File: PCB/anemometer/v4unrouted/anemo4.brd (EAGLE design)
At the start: 100 x 80 mm, 66 parts, among them IC1 AD8223, IC2 AD8223, IC3 AD8223, IC4 AD8223, IC6 TL072D, J1 RJ12STRAIGHT-I2C, J2 RJ12STRAIGHT-I2C

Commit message: put all devices on one side on integrated bertha
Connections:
- net GND renamed AGND
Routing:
- net AGND: track 0.00 -> 27.0 mm
- added copper zone on layer 16, net N$15
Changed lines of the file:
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@@
 <wire x1="62.17" y1="70.485" x2="73.66" y2="72.26" width="0" layer="19" extent="1-1"/>
 </signal>
-<signal name="GND" class="1">
+<signal name="AGND" class="1">
 <contactref element="DIV2" pad="1"/>
 <contactref element="DIV8" pad="1"/>
@@
 <contactref element="LED0" pad="C"/>
 <contactref element="U$1" pad="5"/>
+<wire x1="31.75" y1="75.19" x2="31.75" y2="77.47" width="0.6096" layer="1"/>
+<wire x1="31.75" y1="77.47" x2="13.97" y2="77.47" width="0.6096" layer="1"/>
+<wire x1="13.97" y1="77.47" x2="13.97" y2="73.025" width="0.6096" layer="1"/>
 <wire x1="86.36" y1="66.675" x2="86.36" y2="69.215" width="0" layer="19" extent="1-1"/>
 <wire x1="78.74" y1="75.06" x2="86.36" y2="69.215" width="0" layer="19" extent="1-1"/>
@@
 <wire x1="43.18" y1="76.33" x2="46.99" y2="76.33" width="0" layer="19" extent="1-1"/>
 <wire x1="31.75" y1="75.19" x2="43.18" y2="76.33" width="0" layer="19" extent="1-1"/>
-<wire x1="24.13" y1="68.58" x2="31.75" y2="75.19" width="0" layer="19" extent="1-1"/>
-<wire x1="21.46" y1="73.66" x2="24.13" y2="68.58" width="0" layer="19" extent="16-16"/>
-<wire x1="21.46" y1="77.47" x2="21.46" y2="73.66" width="0" layer="19" extent="16-16"/>
-<wire x1="13.97" y1="73.025" x2="21.46" y2="73.66" width="0" layer="19" extent="16-16"/>
-<wire x1="13.97" y1="70.485" x2="13.97" y2="73.025" width="0" layer="19" extent="1-1"/>
+<wire x1="21.46" y1="77.47" x2="13.97" y2="77.47" width="0" layer="19" extent="1-16"/>
+<wire x1="21.46" y1="73.66" x2="21.46" y2="77.47" width="0" layer="19" extent="16-16"/>
+<wire x1="24.13" y1="68.58" x2="21.46" y2="73.66" width="0" layer="19" extent="16-16"/>
 <wire x1="30.48" y1="63.5" x2="24.13" y2="68.58" width="0" layer="19" extent="1-1"/>
 <wire x1="64.9" y1="53.34" x2="68.35" y2="64.77" width="0" layer="19" extent="1-16"/>
 <wire x1="65.405" y1="50.74" x2="64.9" y2="53.34" width="0" layer="19" extent="1-16"/>
 <wire x1="73.66" y1="50.93" x2="65.405" y2="50.74" width="0" layer="19" extent="1-1"/>
-<wire x1="86.49" y1="53.34" x2="73.66" y2="50.93" width="0" layer="19" extent="1-16"/>
-<wire x1="86.995" y1="50.74" x2="86.49" y2="53.34" width="0" layer="19" extent="1-16"/>
 <wire x1="30.48" y1="50.93" x2="30.48" y2="63.5" width="0" layer="19" extent="1-1"/>
 <wire x1="22.225" y1="50.74" x2="30.48" y2="50.93" width="0" layer="19" extent="1-1"/>
 <wire x1="21.72" y1="53.34" x2="22.225" y2="50.74" width="0" layer="19" extent="1-16"/>
+<wire x1="86.49" y1="53.34" x2="73.66" y2="50.93" width="0" layer="19" extent="1-16"/>
+<wire x1="86.995" y1="50.74" x2="86.49" y2="53.34" width="0" layer="19" extent="1-16"/>
 <wire x1="52.07" y1="50.93" x2="64.9" y2="53.34" width="0" layer="19" extent="1-16"/>
 <wire x1="43.815" y1="50.74" x2="52.07" y2="50.93" width="0" layer="19" extent="1-1"/>
@@
 <wire x1="20.45" y1="30.48" x2="22.225" y2="50.74" width="0" layer="19" extent="1-16"/>
 <wire x1="20.45" y1="16.51" x2="20.45" y2="30.48" width="0" layer="19" extent="16-16"/>
+<wire x1="13.97" y1="73.025" x2="13.97" y2="70.485" width="0.6096" layer="1"/>
 </signal>
 <signal name="IN+1">
@@
 <wire x1="71.35" y1="64.77" x2="74.8" y2="64.77" width="0" layer="19" extent="1-1"/>
 </signal>
+<signal name="N$15">
+<polygon width="0.6096" layer="16" isolate="0.3048" orphans="yes">
+<vertex x="0" y="80.01"/>
+<vertex x="99.695" y="80.01"/>
+<vertex x="99.695" y="0"/>
+<vertex x="0" y="0"/>
+</polygon>
+</signal>
 </signals>

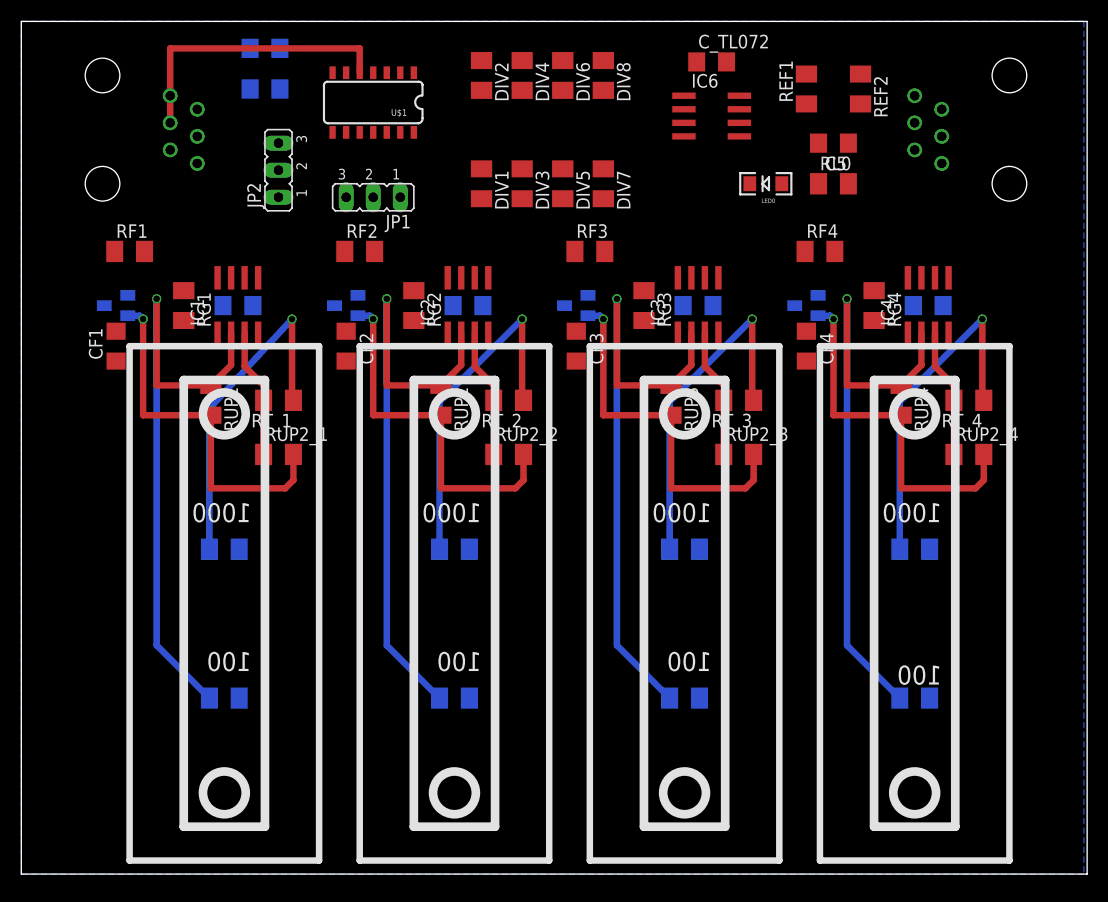
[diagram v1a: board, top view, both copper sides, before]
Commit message: routed anemometer and integrated bertha with ground planes and separate analog and digital ground. ready for fabrication
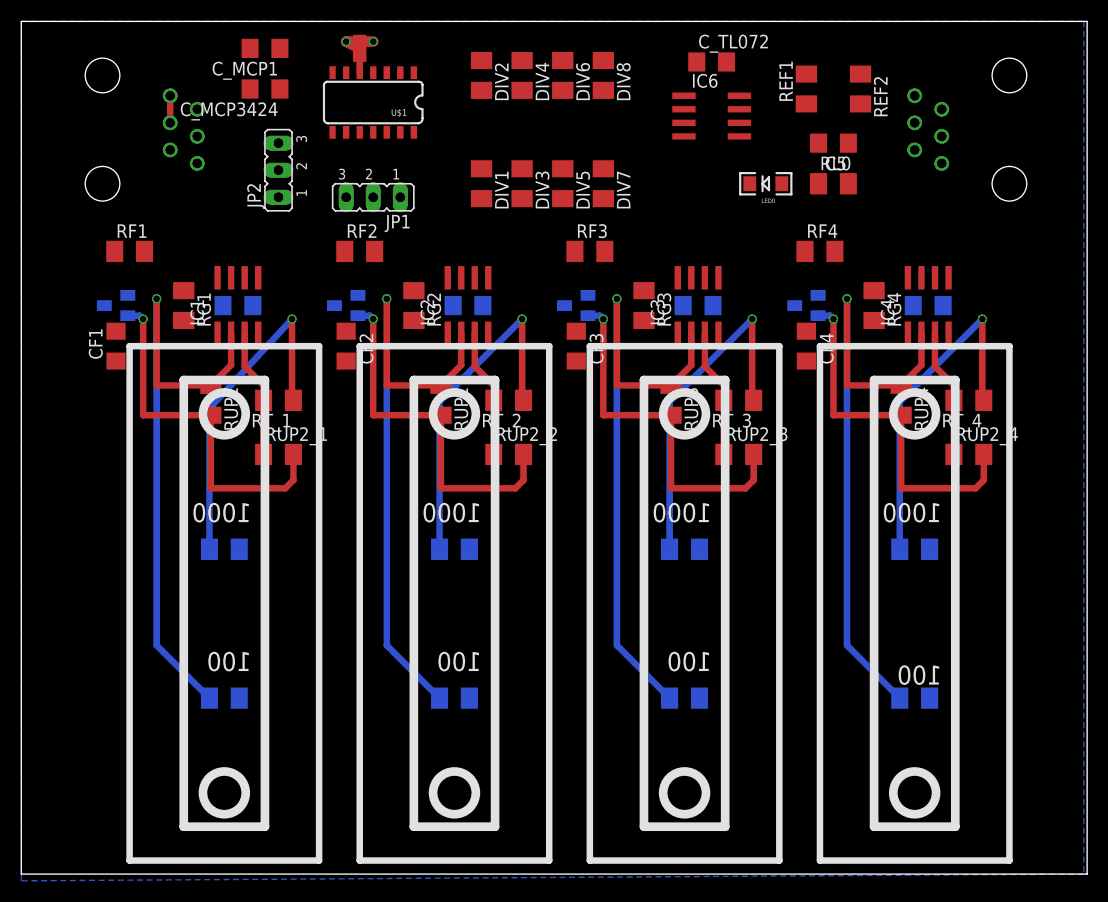
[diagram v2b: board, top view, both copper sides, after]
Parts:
- added U$2: STARGND, lpatiny:STAR
- flipped C_MCP1 to the top
- flipped C_MCP3424 to the top
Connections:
- removed net AGND: C1.2, C2.2, C3.2, C4.2, C5.2, CF1.1, CF2.1, CF3.1, CF4.1, C_MCP1.1, C_MCP3424.1, C_TL072.1, DIV2.1, DIV4.1, DIV6.1, DIV8.1, IC1.4, IC2.4, IC3.4, IC4.4, IC6.4, J1.GND1, J1.GND2, J2.GND1, J2.GND2, JP1.3, JP2.3, LED0.C, PT100_1.1, PT100_2.1, PT100_3.1, PT100_4.1, PT1K_1.1, PT1K_2.1, PT1K_3.1, PT1K_4.1, REF2.1, U$1.5
- new net DGND: U$1.5, U$2.DGND
- new net GND: C1.2, C2.2, C3.2, C4.2, C5.2, CF1.1, CF2.1, CF3.1, CF4.1, C_MCP1.1, C_MCP3424.1, C_TL072.1, DIV2.1, DIV4.1, DIV6.1, DIV8.1, IC1.4, IC2.4, IC3.4, IC4.4, IC6.4, J1.GND1, J1.GND2, J2.GND1, J2.GND2, JP1.3, JP2.3, LED0.C, PT100_1.1, PT100_2.1, PT100_3.1, PT100_4.1, PT1K_1.1, PT1K_2.1, PT1K_3.1, PT1K_4.1, REF2.1, U$2.AGND, U$2.GND
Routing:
- net AGND: track 27.0 -> 0.00 mm
- net GND: track 0.00 -> 7.13 mm, vias 0 -> 2
- net DGND: track 0.00 -> 2.92 mm
- added copper zone on layer 16, net GND
- removed copper zone on layer 16, net N$15

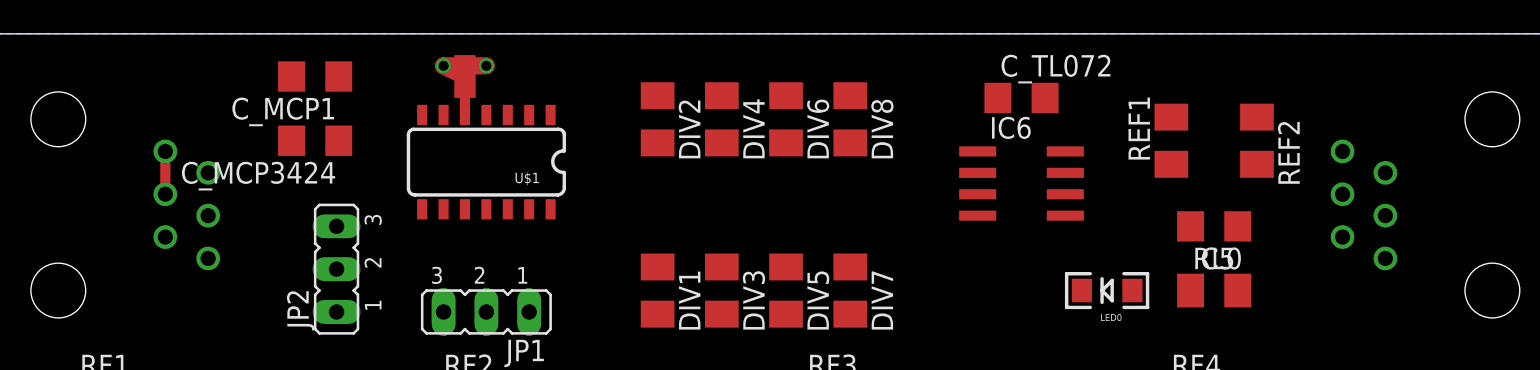
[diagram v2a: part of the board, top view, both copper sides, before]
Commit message: integratedBertha v1.1: adjusted labels to good position. Anemometer: added ferrite bead for vcc decoupling and ground line.
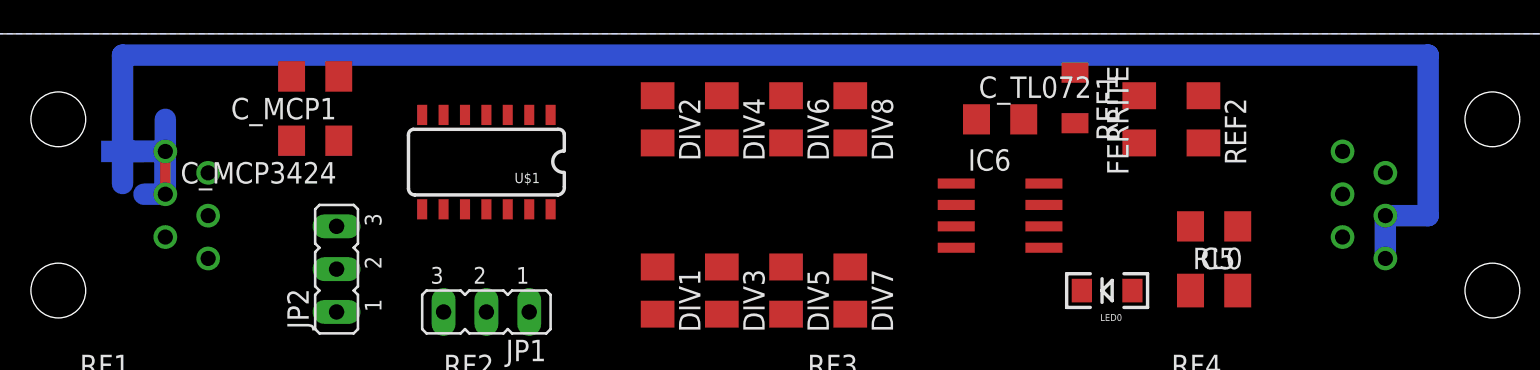
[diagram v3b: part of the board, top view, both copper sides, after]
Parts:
- added FERRITE: 80Ohm, rcl:L3216C
- moved U$2 20.1 mm to (11.4, 73.7), flipped to the bottom, turned to 270 degrees
- moved REF2 3.42 mm to (75.6, 74.9)
- moved REF1 2.29 mm to (71.8, 74.9)
- moved IC6 2.29 mm to (63.5, 69.2)
- moved C_TL072 1.80 mm to (63.5, 74.9)
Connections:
- removed net DGND: U$1.5, U$2.DGND
- new net +12V: FERRITE.1, J1.+12V, J2.+12V
- new net MIXEDGND: J1.GND1, J1.GND2, J2.GND1, J2.GND2, U$2.GND
- net GND: now also U$1.5; no longer J1.GND1, J1.GND2, J2.GND1, J2.GND2, U$2.GND
- net VCC: now also FERRITE.2; no longer J1.+12V, J2.+12V
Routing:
- net MIXEDGND: track 0.00 -> 105.4 mm
- net GND: track 7.13 -> 10.2 mm, vias 2 -> 0
- net DGND: track 2.92 -> 0.00 mm

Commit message: changed some labels, corrected C16 value in bertha. created BOM
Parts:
- PT100_1, PT100_2, PT100_3, PT100_4: value 90.9 -> PT100
- PT1K_1, PT1K_2, PT1K_3, PT1K_4: value 90.9 -> PT1000
- RG1, RG2, RG3, RG4: value 91 -> 91 0.1%
- RT_1, RT_2, RT_3, RT_4: value 90.9 -> 91 0.1%
- RUP1, RUP2, RUP3, RUP4: value 10 -> 10 0.1%
- RUP2_1, RUP2_2, RUP2_3, RUP2_4: value 100 -> 100 0.1%
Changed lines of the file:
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@@
 </autorouter>
 <elements>
-<element name="RG1" library="resistor" package="M1206" value="91" x="15.24" y="53.34" rot="R270"/>
-<element name="RUP1" library="resistor" package="M1206" value="10" x="17.78" y="44.45" rot="R270"/>
-<element name="RG2" library="resistor" package="M1206" value="91" x="36.83" y="53.34" rot="R270"/>
-<element name="RG3" library="resistor" package="M1206" value="91" x="58.42" y="53.34" rot="R270"/>
-<element name="RG4" library="resistor" package="M1206" value="91" x="80.01" y="53.34" rot="R270"/>
-<element name="RUP2" library="resistor" package="M1206" value="10" x="39.37" y="44.45" rot="R270"/>
-<element name="RUP3" library="resistor" package="M1206" value="10" x="60.96" y="44.45" rot="R270"/>
-<element name="RUP4" library="resistor" package="M1206" value="10" x="82.55" y="44.45" rot="R270"/>
-<element name="RUP2_1" library="resistor" package="M1206" value="100" x="24.13" y="39.37"/>
-<element name="RUP2_2" library="resistor" package="M1206" value="100" x="45.72" y="39.37"/>
-<element name="RUP2_3" library="resistor" package="M1206" value="100" x="67.31" y="39.37"/>
-<element name="RUP2_4" library="resistor" package="M1206" value="100" x="88.9" y="39.37"/>
+<element name="RG1" library="resistor" package="M1206" value="91 0.1%" x="15.24" y="53.34" rot="R270"/>
+<element name="RUP1" library="resistor" package="M1206" value="10 0.1%" x="17.78" y="44.45" rot="R270"/>
+<element name="RG2" library="resistor" package="M1206" value="91 0.1%" x="36.83" y="53.34" rot="R270"/>
+<element name="RG3" library="resistor" package="M1206" value="91 0.1%" x="58.42" y="53.34" rot="R270"/>
+<element name="RG4" library="resistor" package="M1206" value="91 0.1%" x="80.01" y="53.34" rot="R270"/>
+<element name="RUP2" library="resistor" package="M1206" value="10 0.1%" x="39.37" y="44.45" rot="R270"/>
+<element name="RUP3" library="resistor" package="M1206" value="10 0.1%" x="60.96" y="44.45" rot="R270"/>
+<element name="RUP4" library="resistor" package="M1206" value="10 0.1%" x="82.55" y="44.45" rot="R270"/>
+<element name="RUP2_1" library="resistor" package="M1206" value="100 0.1%" x="24.13" y="39.37"/>
+<element name="RUP2_2" library="resistor" package="M1206" value="100 0.1%" x="45.72" y="39.37"/>
+<element name="RUP2_3" library="resistor" package="M1206" value="100 0.1%" x="67.31" y="39.37"/>
+<element name="RUP2_4" library="resistor" package="M1206" value="100 0.1%" x="88.9" y="39.37"/>
 <element name="REF1" library="resistor" package="M1206" value="200k" x="71.755" y="74.93" rot="R90"/>
 <element name="REF2" library="resistor" package="M1206" value="100k" x="75.565" y="74.93" rot="R270"/>
-<element name="RT_1" library="resistor" package="M1206" value="90.9" x="24.13" y="44.45" rot="R180"/>
-<element name="RT_2" library="resistor" package="M1206" value="90.9" x="45.72" y="44.45" rot="R180"/>
-<element name="RT_3" library="resistor" package="M1206" value="90.9" x="67.31" y="44.45" rot="R180"/>
-<element name="RT_4" library="resistor" package="M1206" value="90.9" x="88.9" y="44.45" rot="R180"/>
+<element name="RT_1" library="resistor" package="M1206" value="91 0.1%" x="24.13" y="44.45" rot="R180"/>
+<element name="RT_2" library="resistor" package="M1206" value="91 0.1%" x="45.72" y="44.45" rot="R180"/>
+<element name="RT_3" library="resistor" package="M1206" value="91 0.1%" x="67.31" y="44.45" rot="R180"/>
+<element name="RT_4" library="resistor" package="M1206" value="91 0.1%" x="88.9" y="44.45" rot="R180"/>
 <element name="RF1" library="resistor" package="M1206" value="100" x="10.16" y="58.42"/>
 <element name="RF2" library="resistor" package="M1206" value="100" x="31.75" y="58.42"/>
@@
 <element name="C_MCP1" library="rcl" package="C1206" value="10µ" x="22.86" y="77.47" rot="R180"/>
 <element name="U$1" library="mcp3424" package="14LDSOIC" value="MCP3424(SO14)" x="33.02" y="72.39" rot="R270"/>
-<element name="PT1K_1" library="resistor" package="M1206" value="90.9" x="19.05" y="30.48" rot="MR0"/>
-<element name="PT100_1" library="resistor" package="M1206" value="90.9" x="19.05" y="16.51" rot="MR0"/>
-<element name="PT100_2" library="resistor" package="M1206" value="90.9" x="40.64" y="16.51" rot="MR0"/>
-<element name="PT100_3" library="resistor" package="M1206" value="90.9" x="62.23" y="16.51" rot="MR0"/>
-<element name="PT100_4" library="resistor" package="M1206" value="90.9" x="83.82" y="16.51" rot="MR0"/>
-<element name="PT1K_2" library="resistor" package="M1206" value="90.9" x="40.64" y="30.48" rot="MR0"/>
-<element name="PT1K_3" library="resistor" package="M1206" value="90.9" x="62.23" y="30.48" rot="MR0"/>
-<element name="PT1K_4" library="resistor" package="M1206" value="90.9" x="83.82" y="30.48" rot="MR0"/>
+<element name="PT1K_1" library="resistor" package="M1206" value="PT1000" x="19.05" y="30.48" rot="MR0"/>
+<element name="PT100_1" library="resistor" package="M1206" value="PT100" x="19.05" y="16.51" rot="MR0"/>
+<element name="PT100_2" library="resistor" package="M1206" value="PT100" x="40.64" y="16.51" rot="MR0"/>
+<element name="PT100_3" library="resistor" package="M1206" value="PT100" x="62.23" y="16.51" rot="MR0"/>
+<element name="PT100_4" library="resistor" package="M1206" value="PT100" x="83.82" y="16.51" rot="MR0"/>
+<element name="PT1K_2" library="resistor" package="M1206" value="PT1000" x="40.64" y="30.48" rot="MR0"/>
+<element name="PT1K_3" library="resistor" package="M1206" value="PT1000" x="62.23" y="30.48" rot="MR0"/>
+<element name="PT1K_4" library="resistor" package="M1206" value="PT1000" x="83.82" y="30.48" rot="MR0"/>
 <element name="IC1" library="analog-devices" package="SO8" value="AD8223" x="20.32" y="53.34">
 <attribute name="OC_NEWARK" value="05F7109" x="20.32" y="53.34" size="1.778" layer="27" display="off"/>
